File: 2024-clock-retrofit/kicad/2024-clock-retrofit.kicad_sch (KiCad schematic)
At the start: 13 parts, among them SW1 SW_Push, U1 ESP32-WROOM-32

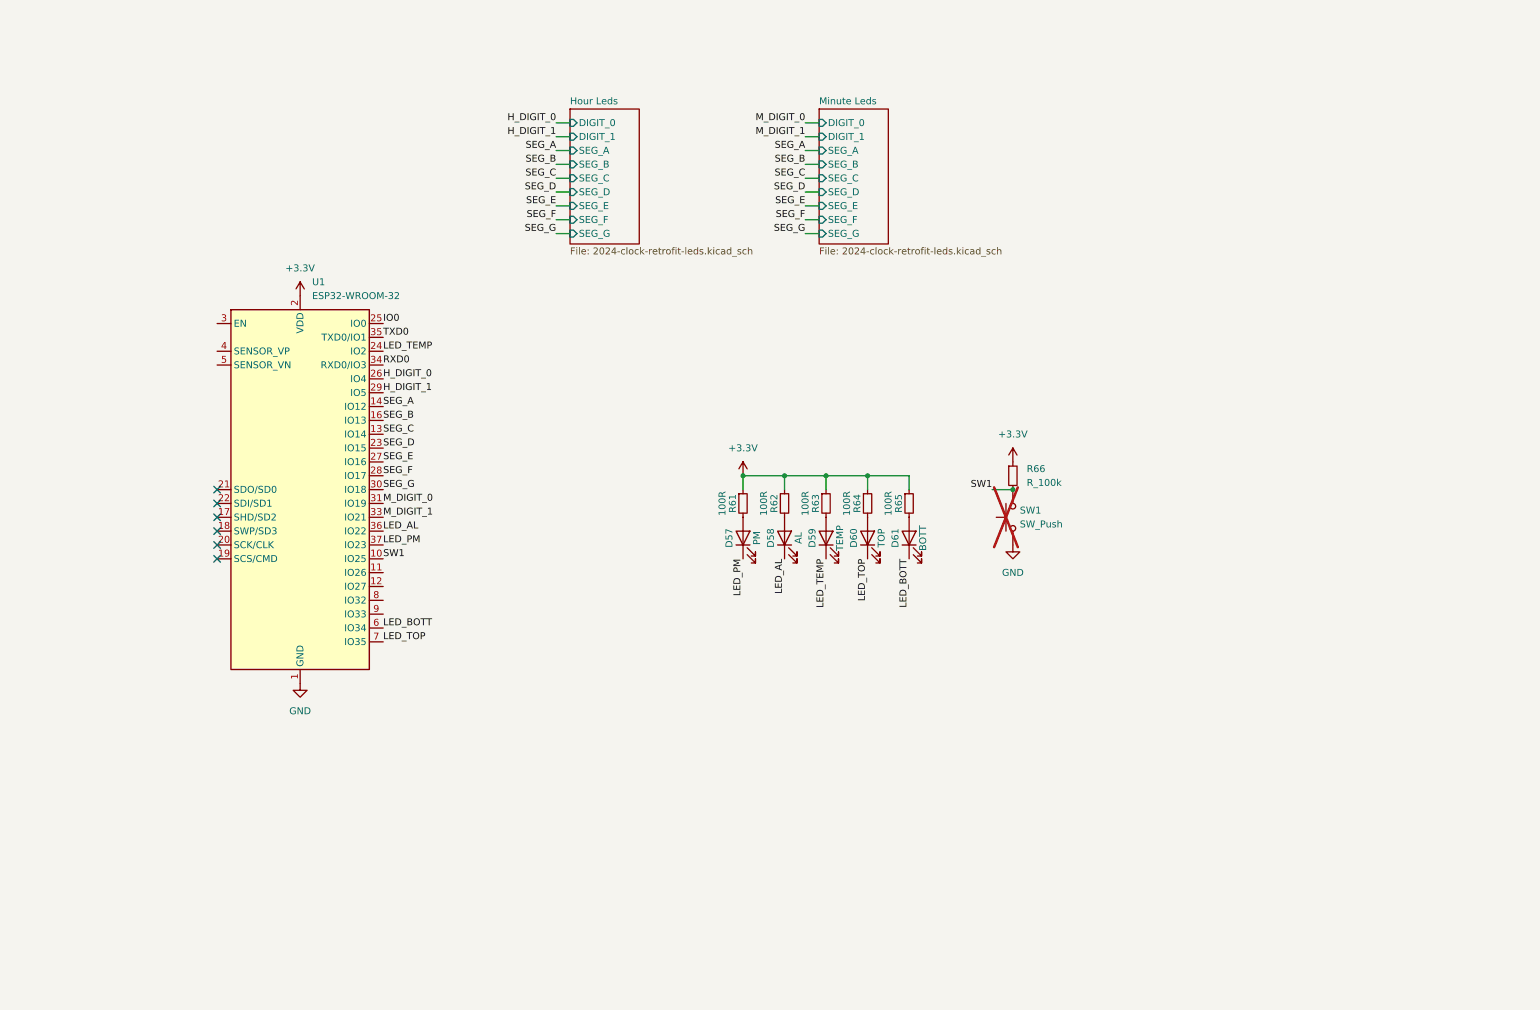
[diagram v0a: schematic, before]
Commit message: 2024-clock-retrofit: ready for jlcpcb
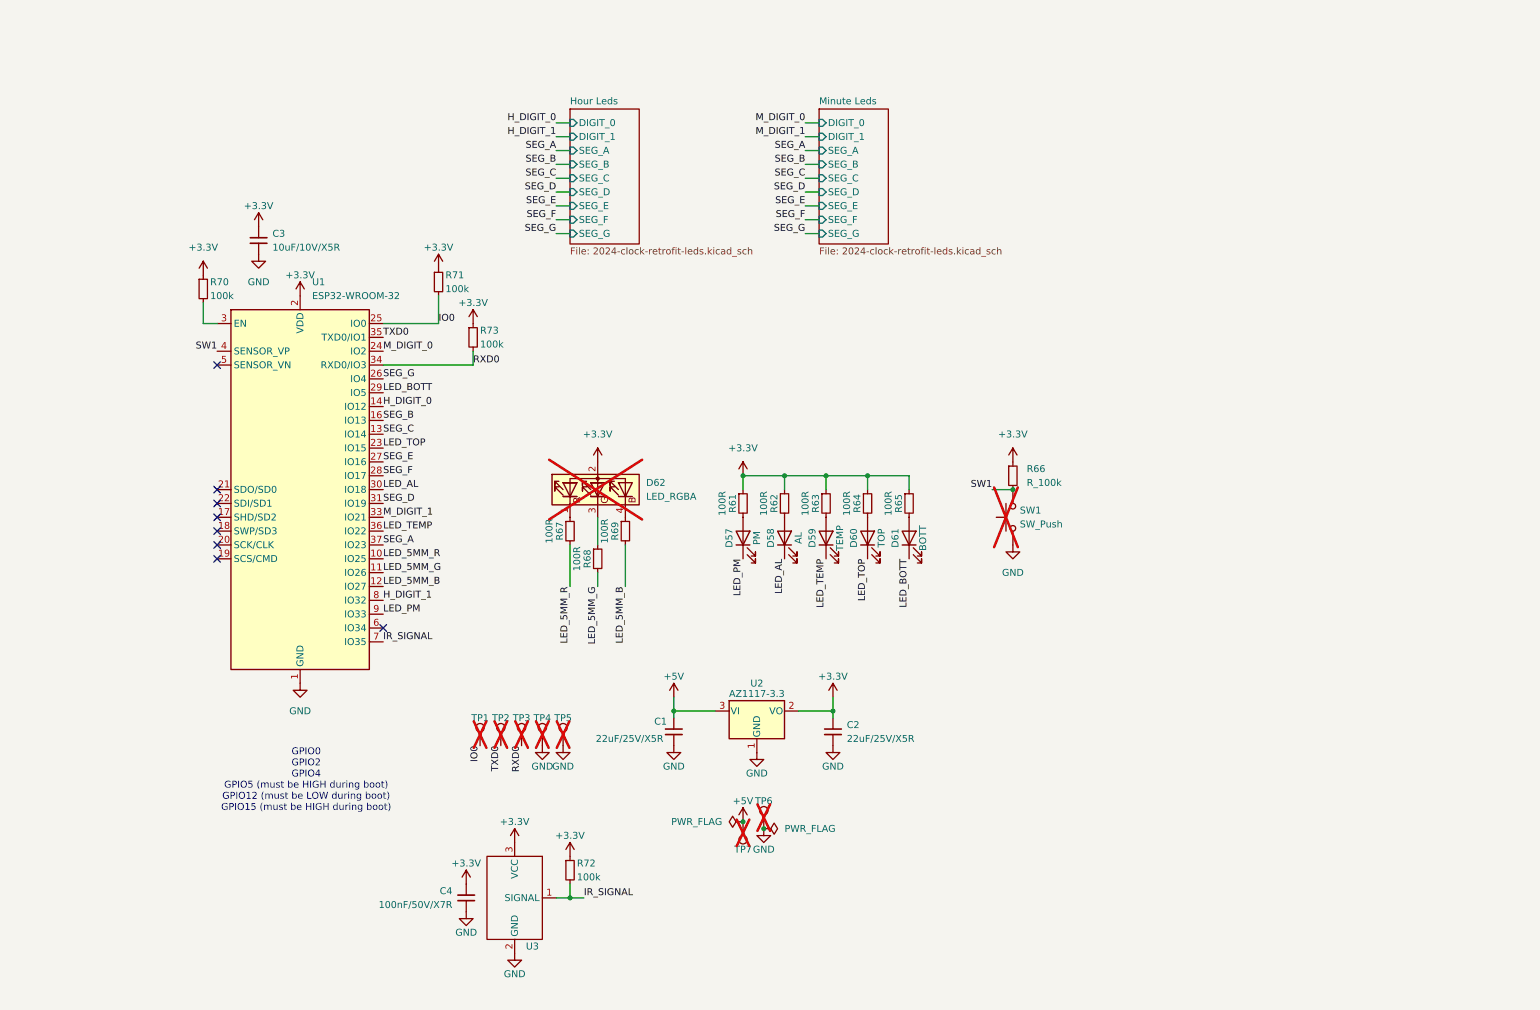
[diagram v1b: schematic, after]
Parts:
- added C1, C2: 22uF/25V/X5R, library:C_1206_3216Metric, symbol library:10uF,25V,X5R
- added C3: 10uF/10V/X5R, library:C_0603_1608Metric, symbol library:10uF,10V,X5R
- added C4: 100nF/50V/X7R, library:C_0603_1608Metric, symbol library:100nF/50V/X7R
- added D62: LED_RGBA, library:LED_D5.0mm-4_RGB, symbol library:LED_RGBA
- added R67, R68, R69: 100R, library:R_0402_1005Metric, symbol library:R_100R
- added R70, R71, R72, R73: 100k, library:R_0402_1005Metric, symbol library:R_100k
- added TP1, TP2, TP3, TP4, TP5, TP6, TP7: TestPoint, library:TestPoint_Pad_D2.0mm, symbol library:TestPoint
- added U2: AZ1117-3.3, library:SOT-223-3_TabPin2, symbol library:AZ1117-1.2
- added U3: ~, library:IR_RECEIVER, symbol library:IR_RECEIVER
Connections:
- net +3.3V: now also C2.1, C3.1, C4.1, D62.2 (A), R70.1, R71.1, R72.1, R73.1, U2.2 (VO), U3.3 (VCC)
- net GND: now also C1.2, C2.2, C3.2, C4.2, TP4.1, TP5.1, TP6.1, U2.1 (GND), U3.2 (GND)
- net H_DIGIT_0: now also U1.14 (IO12); no longer U1.26 (IO4)
- net H_DIGIT_1: now also U1.8 (IO32); no longer U1.29 (IO5)
- net IO0: now also R71.2, TP1.1
- net LED_AL: now also U1.30 (IO18); no longer U1.36 (IO22)
- net LED_BOTT: now also U1.29 (IO5); no longer U1.6 (IO34)
- net LED_PM: now also U1.9 (IO33); no longer U1.37 (IO23)
- net LED_TEMP: now also U1.36 (IO22); no longer U1.24 (IO2)
- net LED_TOP: now also U1.23 (IO15); no longer U1.7 (IO35)
- net M_DIGIT_0: now also U1.24 (IO2); no longer U1.31 (IO19)
- net RXD0: now also R73.2, TP3.1
- net SEG_A: now also U1.37 (IO23); no longer U1.14 (IO12)
- net SEG_D: now also U1.31 (IO19); no longer U1.23 (IO15)
- net SEG_G: now also U1.26 (IO4); no longer U1.30 (IO18)
- net SW1: now also U1.4 (SENSOR_VP); no longer U1.10 (IO25)
- net TXD0: now also TP2.1
- net LED_5MM_G: now reaches U1.11 (IO26)
- net LED_5MM_G: now also R68.2
- net LED_5MM_B: now reaches U1.12 (IO27)
- net LED_5MM_B: now also R69.2
- net at U1.3 (EN): now also R70.2
- new net: D62.1 (RK), R67.1
- new net: D62.4 (BK), R69.1
- new net: D62.3 (GK), R68.1
- new net +5V: C1.1, TP7.1, U2.3 (VI)
- new net IR_SIGNAL: R72.2, U1.7 (IO35), U3.1 (SIGNAL)
- new net LED_5MM_R: R67.2, U1.10 (IO25)
- no-connect marks 6 -> 8
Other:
- note added: "GPIO0 GPIO2 GPIO4 GPIO5 (must be HIGH during boot) GPIO12 (must be LOW during boot) GPIO15 (must be HIGH during boot)"

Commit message: 2024-clock-retrofit: fix rotation to match jlc
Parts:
- U1, U3: now not fitted; now left out of the parts list
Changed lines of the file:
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@@
 		(unit 1)
 		(exclude_from_sim no)
-		(in_bom yes)
-		(on_board yes)
-		(dnp no)
+		(in_bom no)
+		(on_board yes)
+		(dnp yes)
 		(fields_autoplaced yes)
 		(property "Reference" "U1"
@@
 		(unit 1)
 		(exclude_from_sim no)
-		(in_bom yes)
-		(on_board yes)
-		(dnp no)
+		(in_bom no)
+		(on_board yes)
+		(dnp yes)
 		(property "Reference" "U3"
 			(at 111.125 184.15 0)

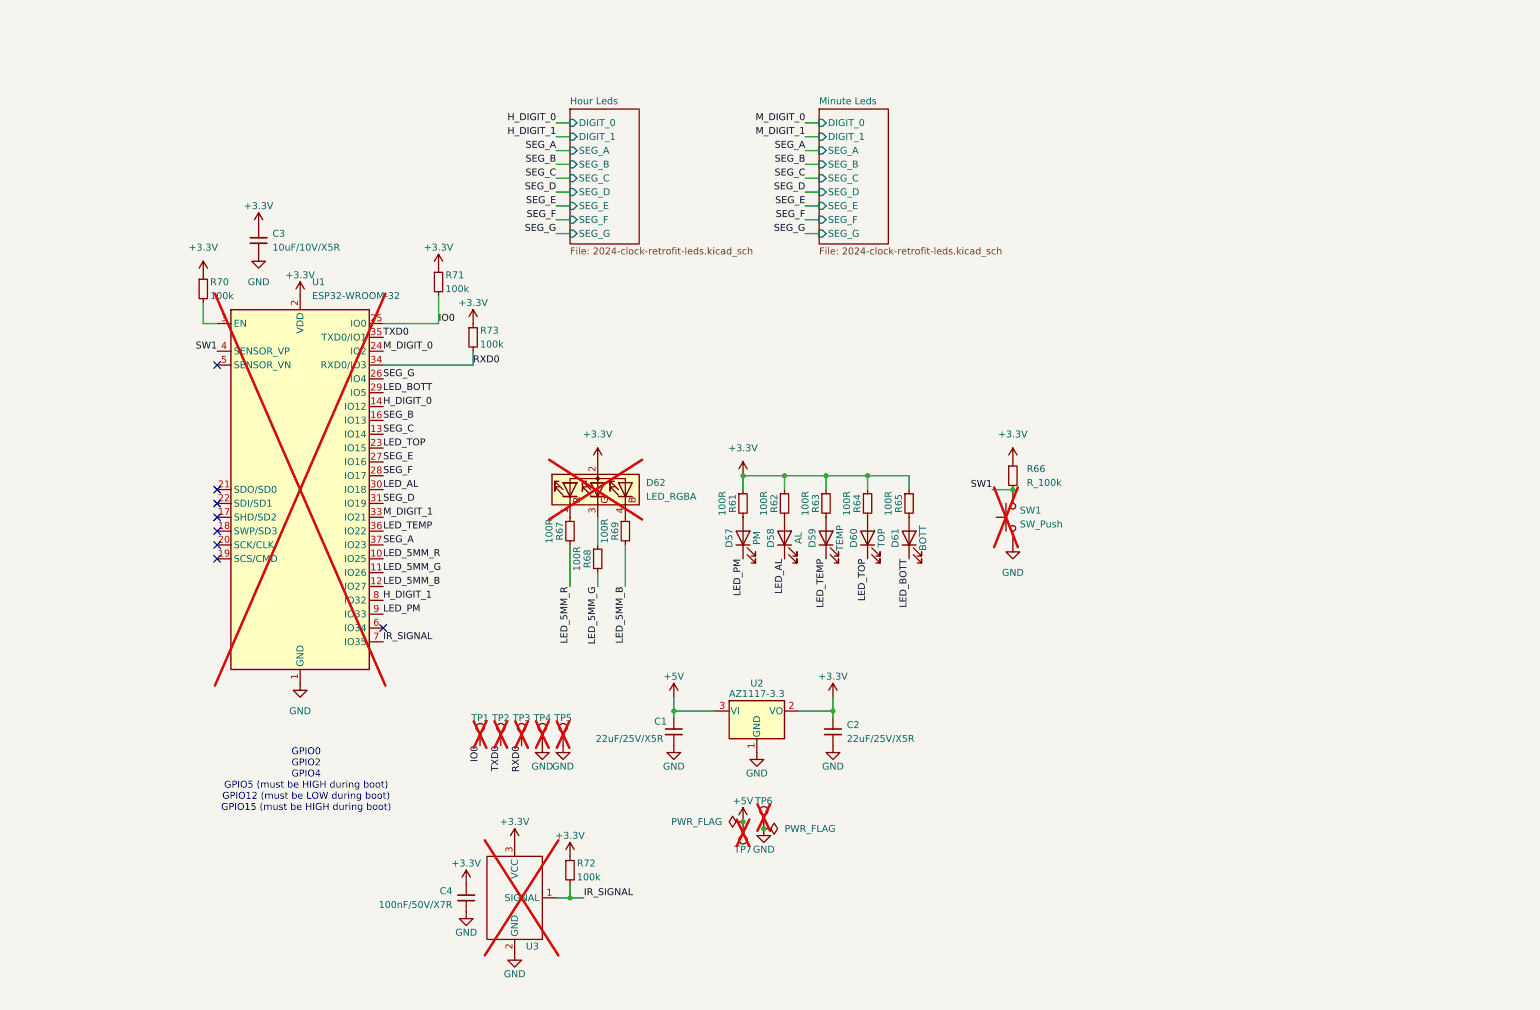
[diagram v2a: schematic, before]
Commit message: 2024-clock-retrofit: as submitted April 2025
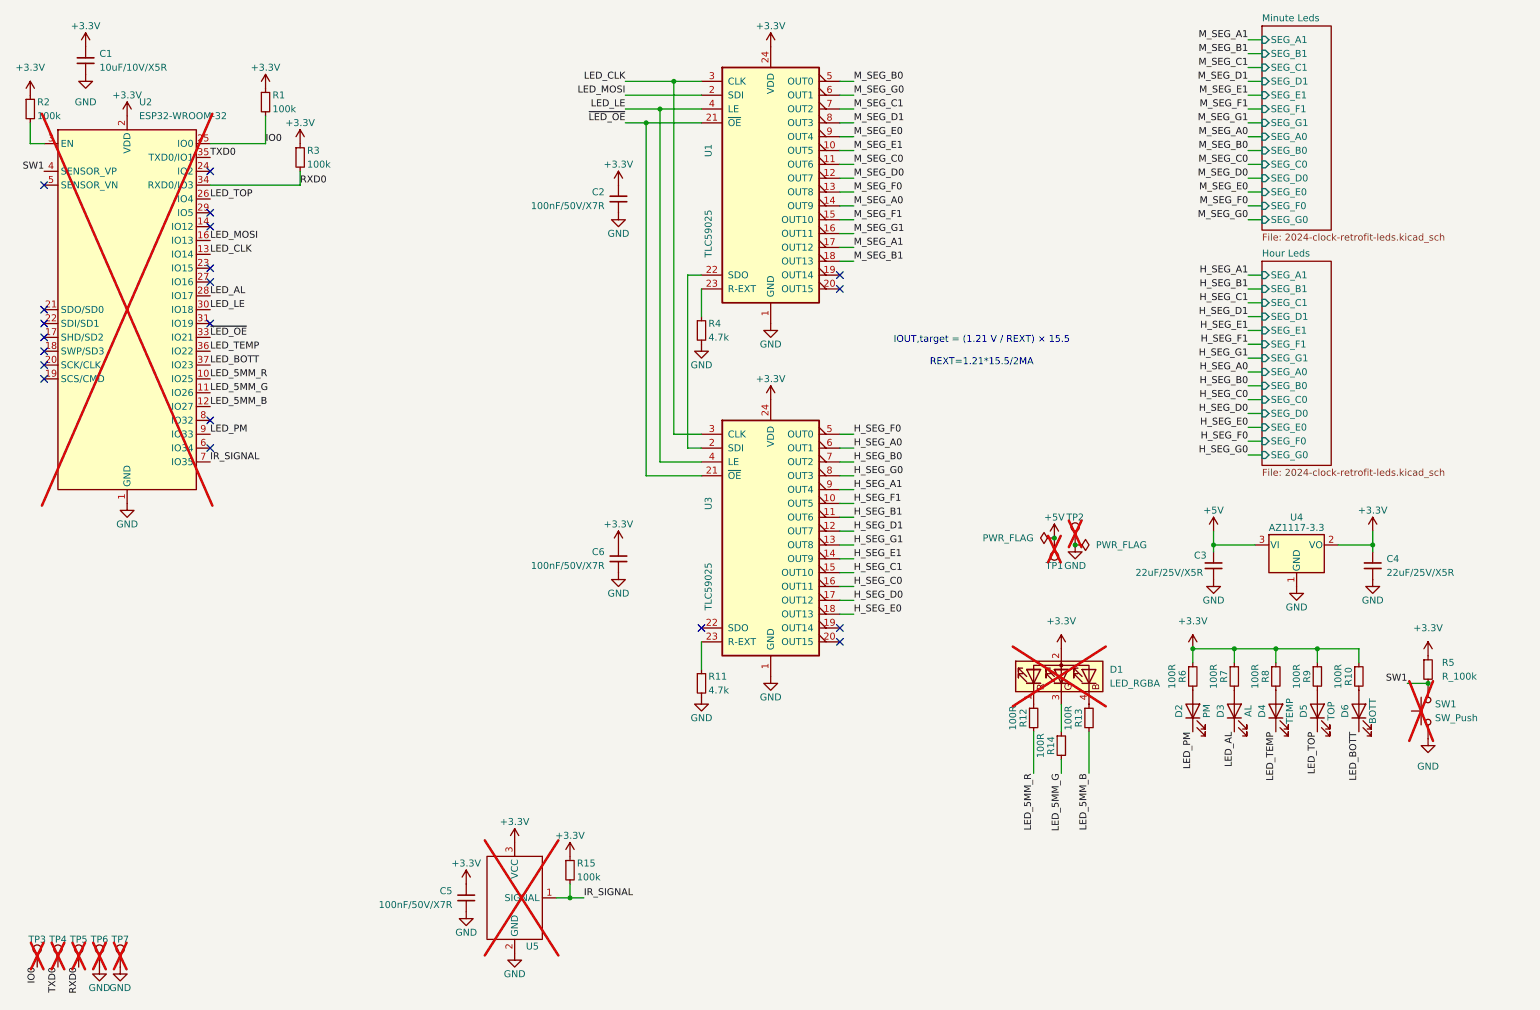
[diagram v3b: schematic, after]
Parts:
- added C2, C6: 100nF/50V/X7R, library:C_0603_1608Metric, symbol library:100nF/50V/X7R
- added R11, R4: 4.7k, library:R_0805_2012Metric, symbol library:R_100k
- added U1, U3: TLC59025, library:SSOP-24_3.9x8.7mm_P0.635mm, symbol library:TLC59025-gkl_misc
- renumbered C3 to C1, C1 to C3, C2 to C4, C4 to C5, D62 to D1, D57 to D2, D58 to D3, D59 to D4, D60 to D5, D61 to D6, R71 to R1, R65 to R10, R67 to R12, R69 to R13, R68 to R14, R72 to R15, R70 to R2, R73 to R3, R66 to R5, R61 to R6, R62 to R7, R63 to R8, R64 to R9, TP7 to TP1, TP6 to TP2, TP1 to TP3, TP2 to TP4, TP3 to TP5, TP4 to TP6, TP5 to TP7, U1 to U2, U2 to U4, U3 to U5
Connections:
- net SEG_A is gone; now on net LED_BOTT: U2.37 (IO23)
- net SEG_F is gone; now on net LED_AL: U2.28 (IO17)
- net SEG_G is gone; now on net LED_TOP: U2.26 (IO4)
- net +3.3V: now also C2.1, C6.1, U1.24 (VDD), U3.24 (VDD)
- net GND: now also C2.2, C6.2, R11.2, R4.2, U1.1 (GND), U3.1 (GND)
- net LED_AL: no longer U2.30 (IO18)
- net LED_BOTT: no longer U2.29 (IO5)
- net LED_TOP: no longer U2.23 (IO15)
- net H_DIGIT_0: no longer names the net of U2.14 (IO12)
- net H_DIGIT_1: no longer names the net of U2.8 (IO32)
- net M_DIGIT_0: no longer names the net of U2.24 (IO2)
- net M_DIGIT_1 renamed ~{LED_OE}
- net ~{LED_OE}: now also U1.21 (~{OE}), U3.21 (~{OE})
- net SEG_B renamed LED_MOSI
- net LED_MOSI: now also U1.2 (SDI)
- net SEG_C renamed LED_CLK
- net LED_CLK: now also U1.3 (CLK), U3.3 (CLK)
- net SEG_D: no longer names the net of U2.31 (IO19)
- net SEG_E: no longer names the net of U2.27 (IO16)
- new net: U1.22 (SDO), U3.2 (SDI)
- new net: R11.1, U3.23 (R-EXT)
- new net: R4.1, U1.23 (R-EXT)
- new net H_SEG_A0: U3.6 (OUT1)
- new net H_SEG_A1: U3.9 (OUT4)
- new net H_SEG_B0: U3.7 (OUT2)
- new net H_SEG_B1: U3.11 (OUT6)
- new net H_SEG_C0: U3.16 (OUT11)
- new net H_SEG_C1: U3.15 (OUT10)
- new net H_SEG_D0: U3.17 (OUT12)
- new net H_SEG_D1: U3.12 (OUT7)
- new net H_SEG_E0: U3.18 (OUT13)
- new net H_SEG_E1: U3.14 (OUT9)
- new net H_SEG_F0: U3.5 (OUT0)
- new net H_SEG_F1: U3.10 (OUT5)
- new net H_SEG_G0: U3.8 (OUT3)
- new net H_SEG_G1: U3.13 (OUT8)
- new net LED_LE: U1.4 (LE), U2.30 (IO18), U3.4 (LE)
- new net M_SEG_A0: U1.14 (OUT9)
- new net M_SEG_A1: U1.17 (OUT12)
- new net M_SEG_B0: U1.5 (OUT0)
- new net M_SEG_B1: U1.18 (OUT13)
- new net M_SEG_C0: U1.11 (OUT6)
- new net M_SEG_C1: U1.7 (OUT2)
- new net M_SEG_D0: U1.12 (OUT7)
- new net M_SEG_D1: U1.8 (OUT3)
- new net M_SEG_E0: U1.9 (OUT4)
- new net M_SEG_E1: U1.10 (OUT5)
- new net M_SEG_F0: U1.13 (OUT8)
- new net M_SEG_F1: U1.15 (OUT10)
- new net M_SEG_G0: U1.6 (OUT1)
- new net M_SEG_G1: U1.16 (OUT11)
- no-connect marks 8 -> 20
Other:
- sheet Hour Leds ports: added SEG_A0, SEG_A1, SEG_B0, SEG_B1, SEG_C0, SEG_C1, SEG_D0, SEG_D1, SEG_E0, SEG_E1, SEG_F0, SEG_F1, SEG_G0, SEG_G1; removed DIGIT_0, DIGIT_1, SEG_A, SEG_B, SEG_C, SEG_D, SEG_E, SEG_F, SEG_G
- sheet Minute Leds ports: added SEG_A0, SEG_A1, SEG_B0, SEG_B1, SEG_C0, SEG_C1, SEG_D0, SEG_D1, SEG_E0, SEG_E1, SEG_F0, SEG_F1, SEG_G0, SEG_G1; removed DIGIT_0, DIGIT_1, SEG_A, SEG_B, SEG_C, SEG_D, SEG_E, SEG_F, SEG_G
- note added: "IOUT,target = (1.21 V / REXT) × 15.5 REXT=1.21*15.5/2MA"
- note removed: "GPIO0 GPIO2 GPIO4 GPIO5 (must be HIGH during boot) GPIO12 (must be LOW during boot) GPIO15 (must be HIGH during boot)"
- moved on the sheet: C1, C3, C4, D1, D2, D3, D4, D5, D6, R1, R10, R12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
